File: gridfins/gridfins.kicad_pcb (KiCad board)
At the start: 4 copper layers, 155 parts, among them IC1 2536030320001, J1 RBUS, J2 USB_C_Receptacle_USB2.0, J3 ServoCH0, J4 ServoCH1, J5 ServoCH2, J6 ST1W008S4TR2000, J7 Conn_01x06_Pin, Q1 SSM3K15AMFV,L3F, Q3 DMP3099, Q5 BSZ025N04LS, Q6 BSZ025N04LS, U1 ESP32-S3, U10 LM74810, U2 SN65HVD230, U3 LM66200DRLR, U4 MAX77827AEFD+T, U5 SC4215ASTRT, U6 SiC437AED-T1, U8 MMC5983MA, U9 H3LIS331DLTR, Y1 R940000171

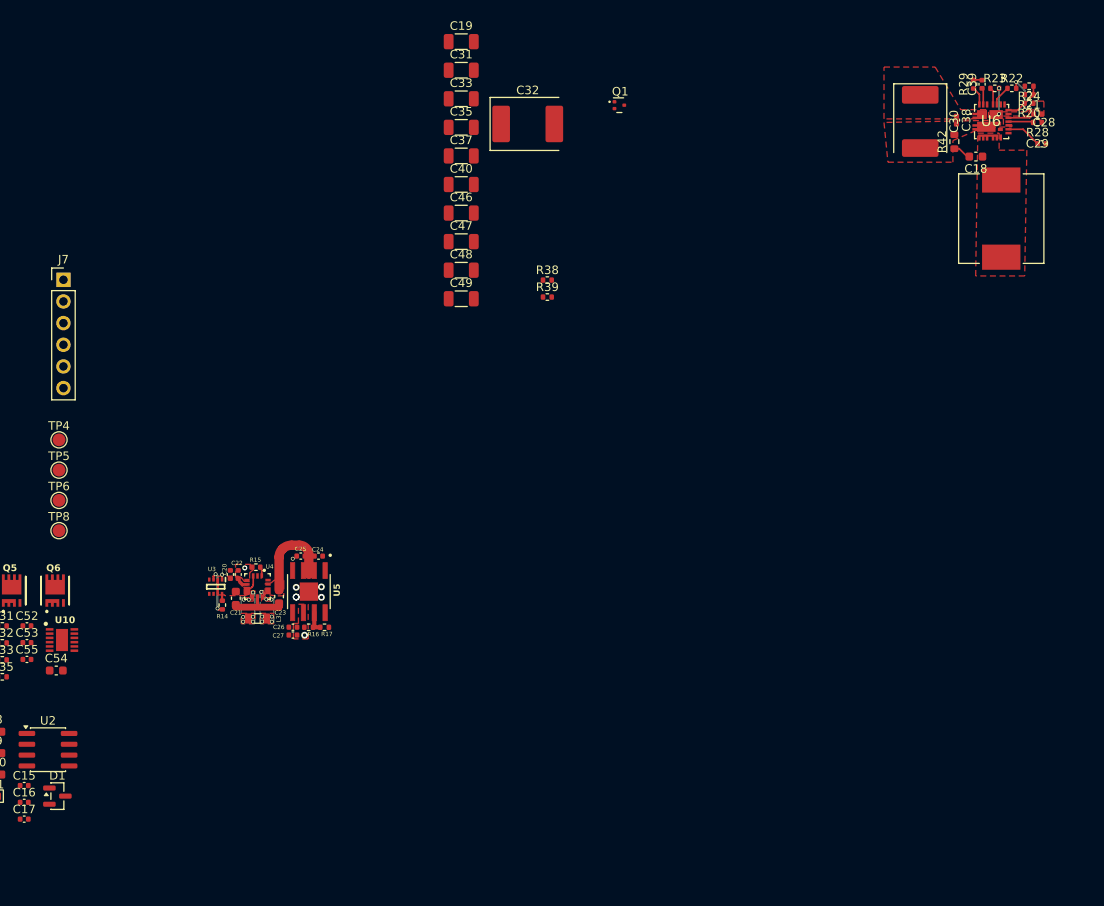
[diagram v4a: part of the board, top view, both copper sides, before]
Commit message: PCB + schematic updates
Solved footprint error which prevented PCB from updating

Deleted old buck converter PCB design (old buck now replaced with 2 for servo and linear acc)

Moved Snubber and crossed out capacitor network to the backside of board

Unsure whether if the +10V routing is valid - currently connected via tracers, not planes (may be a problem for current)

Restructured old pcb which previously had planes associated with no nets (assigned nets to them)

If current design approved, will proceed to carry out the same design for the servo controlling buck converter.
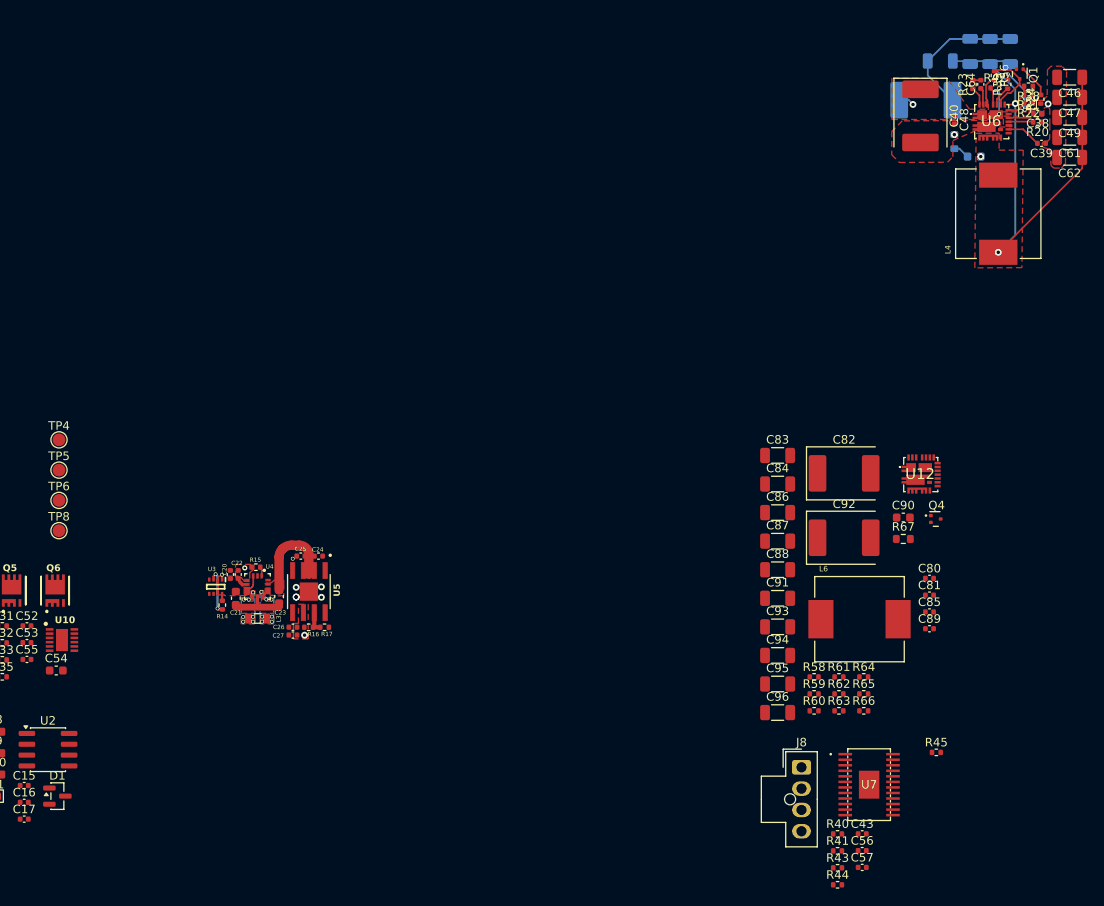
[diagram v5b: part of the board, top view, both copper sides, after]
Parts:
- removed C18: 160pF, Capacitor_SMD:C_0603_1608Metric
- removed C19, C31, C33, C35, C37: 47uF, Capacitor_SMD:C_1206_3216Metric
- removed C28: 1uF, Capacitor_SMD:C_0402_1005Metric
- removed C29: 4.7uF, Capacitor_SMD:C_0402_1005Metric
- removed C30, C32: 100uF, Capacitor_Tantalum_SMD:CP_EIA-7360-38_Kemet-E
- removed J7: Conn_01x06_Pin, Connector_PinHeader_2.54mm:PinHeader_1x06_P2.54mm_Vertical
- removed R28: 10k, Resistor_SMD:R_0402_1005Metric
- removed R29: 2.2, Resistor_SMD:R_0402_1005Metric
- added C43: 10uF, Capacitor_SMD:C_0402_1005Metric, F.Cu at (243.9, 116.0)
- added C56: 0.01uF, Capacitor_SMD:C_0402_1005Metric, F.Cu at (243.9, 118.0)
- added C57: 2.2uF, Capacitor_SMD:C_0402_1005Metric, F.Cu at (243.9, 120.0)
- added C61: 47uF, Capacitor_SMD:C_1206_3216Metric, F.Cu at (268.2, 34.3)
- added C62: 47uF, Capacitor_SMD:C_1206_3216Metric, F.Cu at (268.2, 36.7)
- added C64: 0.1uF, Capacitor_SMD:C_0402_1005Metric, F.Cu at (257.8, 28.1)
- added C65: 160pF, Capacitor_SMD:C_0603_1608Metric, B.Cu at (257.0, 36.6)
- added C75: 100uF, Capacitor_Tantalum_SMD:CP_EIA-7360-38_Kemet-E, B.Cu at (251.3, 30.0)
- added C76: 47uF, Capacitor_SMD:C_1206_3216Metric, B.Cu at (253.0, 25.4)
- added C77: 47uF, Capacitor_SMD:C_1206_3216Metric, B.Cu at (256.5, 24.3)
- added C78: 47uF, Capacitor_SMD:C_1206_3216Metric, B.Cu at (258.9, 24.3)
- added C79: 47uF, Capacitor_SMD:C_1206_3216Metric, B.Cu at (261.2, 24.3)
- added C80: 1uF, Capacitor_SMD:C_0402_1005Metric, F.Cu at (251.8, 86.0)
- added C81: 4.7uF, Capacitor_SMD:C_0402_1005Metric, F.Cu at (251.8, 88.0)
- added C82: 100uF, Capacitor_Tantalum_SMD:CP_EIA-7360-38_Kemet-E, F.Cu at (241.8, 73.7)
- added C83: 47uF, Capacitor_SMD:C_1206_3216Metric, F.Cu at (233.9, 71.6)
- added C84: 47uF, Capacitor_SMD:C_1206_3216Metric, F.Cu at (233.9, 75.0)
- added C85: 100nF, Capacitor_SMD:C_0402_1005Metric, F.Cu at (251.8, 90.0)
- added C86: 47uF, Capacitor_SMD:C_1206_3216Metric, F.Cu at (233.9, 78.3)
- added C87: 47uF, Capacitor_SMD:C_1206_3216Metric, F.Cu at (233.9, 81.7)
- added C88: 47uF, Capacitor_SMD:C_1206_3216Metric, F.Cu at (233.9, 85.0)
- added C89: 0.1uF, Capacitor_SMD:C_0402_1005Metric, F.Cu at (251.8, 92.0)
- added C90: 160pF, Capacitor_SMD:C_0603_1608Metric, F.Cu at (248.7, 78.9)
- added C91: 47uF, Capacitor_SMD:C_1206_3216Metric, F.Cu at (233.9, 88.4)
- added C92: 100uF, Capacitor_Tantalum_SMD:CP_EIA-7360-38_Kemet-E, F.Cu at (241.8, 81.3)
- added C93: 47uF, Capacitor_SMD:C_1206_3216Metric, F.Cu at (233.9, 91.7)
- added C94: 47uF, Capacitor_SMD:C_1206_3216Metric, F.Cu at (233.9, 95.1)
- added C95: 47uF, Capacitor_SMD:C_1206_3216Metric, F.Cu at (233.9, 98.4)
- added C96: 47uF, Capacitor_SMD:C_1206_3216Metric, F.Cu at (233.9, 101.8)
- added J8: 1053131104, Connector_Molex:Molex_Nano-Fit_105309-xx04_1x04_P2.50mm_Vertical, F.Cu at (236.8, 108.2)
- added L6: 3.3uH, iclr:IND_SPM10065VT-3R3M-D, F.Cu at (243.6, 90.8)
- added Q4: SSM3K15AMFV,L3F, iclr:SOT-723, F.Cu at (252.5, 79.1)
- added R40: 51K, Resistor_SMD:R_0402_1005Metric, F.Cu at (241.0, 116.0)
- added R41: 51K, Resistor_SMD:R_0402_1005Metric, F.Cu at (241.0, 118.0)
- added R43: 0.32, Resistor_SMD:R_0402_1005Metric, F.Cu at (241.0, 120.0)
- added R44: 0.32, Resistor_SMD:R_0402_1005Metric, F.Cu at (241.0, 122.0)
- added R45: 18k, Resistor_SMD:R_0402_1005Metric, F.Cu at (252.6, 106.5)
- added R56: 10k, Resistor_SMD:R_0402_1005Metric, F.Cu at (259.4, 27.1)
- added R57: 5.1R, Resistor_SMD:R_0603_1608Metric, B.Cu at (254.7, 34.8)
- added R58: 10k, Resistor_SMD:R_0402_1005Metric, F.Cu at (238.2, 97.6)
- added R59: 113k, Resistor_SMD:R_0402_1005Metric, F.Cu at (238.2, 99.6)
- added R60: 10k, Resistor_SMD:R_0402_1005Metric, F.Cu at (238.2, 101.6)
- added R61: 2.2, Resistor_SMD:R_0402_1005Metric, F.Cu at (241.1, 97.6)
- added R62: 1k, Resistor_SMD:R_0402_1005Metric, F.Cu at (241.1, 99.6)
- added R63: 442k, Resistor_SMD:R_0402_1005Metric, F.Cu at (241.1, 101.6)
- added R64: 200k, Resistor_SMD:R_0402_1005Metric, F.Cu at (244.1, 97.6)
- added R65: 100k, Resistor_SMD:R_0402_1005Metric, F.Cu at (244.1, 99.6)
- added R66: 10k, Resistor_SMD:R_0402_1005Metric, F.Cu at (244.1, 101.6)
- added R67: 5.1R, Resistor_SMD:R_0603_1608Metric, F.Cu at (248.7, 81.4)
- added U12: SiC437AED-T1, iclr:SiC437BEDT1GE3, F.Cu at (250.7, 73.9)
- added U7: DRV8834PWP, iclr:PWP_24, F.Cu at (244.7, 110.2)
- C38: value 100nF -> 1uF
- C39: value 0.1uF -> 4.7uF
- C40: value 47uF -> 100uF; footprint Capacitor_SMD:C_1206_3216Metric -> Capacitor_Tantalum_SMD:CP_EIA-7360-38_Kemet-E
- C48: value 47uF -> 100nF; footprint Capacitor_SMD:C_1206_3216Metric -> Capacitor_SMD:C_0402_1005Metric
- R21: value 113k -> 157k
- R22: value 200k -> 10k
- R23: value 100k -> 2.2
- R24: value 442k -> 1k
- R38: value 10k -> 442k
- R39: value 1k -> 200k
- R42: value 5.1R -> 100k; footprint Resistor_SMD:R_0603_1608Metric -> Resistor_SMD:R_0402_1005Metric
- moved C49 74.5 mm to (268.2, 32.0), turned to 180 degrees
- moved C47 73.3 mm to (268.2, 29.6), turned to 180 degrees
- moved C46 73.1 mm to (268.2, 27.3), turned to 180 degrees
- moved R38 60.8 mm to (263.4, 28.3), turned to 180 degrees
- moved C48 60.5 mm to (254.7, 32.3), turned to -90 degrees
- moved R39 59.5 mm to (260.9, 28.1), turned to 90 degrees
- moved C40 54.5 mm to (250.7, 31.8), turned to -90 degrees
- moved Q1 47.1 mm to (262.4, 26.9), turned to -90 degrees
- moved C39 9.83 mm to (264.9, 35.0), turned to 180 degrees
- moved C38 9.55 mm to (264.4, 31.5), turned to 180 degrees
- moved R42 7.89 mm to (259.4, 28.5), turned to 0 degrees
- moved R22 2.62 mm to (263.4, 30.3), turned to 180 degrees
- moved R23 2.60 mm to (256.9, 28.1), turned to 90 degrees
- moved R20 2.42 mm to (264.4, 32.5)
- moved R24 2.04 mm to (264.8, 29.9), turned to 90 degrees
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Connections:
- net /Buck/SW renamed /Buck_H_bridge/SW
- C38 pad 1: /VOUTSwitch -> GND
- C38 pad 2: GND -> /Buck_H_bridge/VDD
- C39 pad 1: /Buck/BOOT -> GND
- C39 pad 2: Net-(C39-Pad2) -> Net-(U6-V_DRV)
- C40 pad 1: +7.4V -> +16.8V
- C46 pad 1: +7.4V -> +10V
- C47 pad 1: +7.4V -> +10V
- C48 pad 1: +7.4V -> +16.8V
- C49 pad 1: +7.4V -> +10V
- C52 pad 1: +16.8V -> +10V
- L4 pad 1: +7.4V -> +10V
- Q1 pad 3: /Buck/EN -> /Buck_H_bridge/EN
- Q5 pad 1: +16.8V -> +10V
- Q5 pad 2: +16.8V -> +10V
- Q5 pad 3: +16.8V -> +10V
- Q5 pad A1: +16.8V -> +10V
- R20 pad 1: GND -> /Buck_H_bridge/VDD
- R20 pad 2: /Buck/FB -> /BuckPGOOD
- R21 pad 1: /Buck/FB -> /Buck_H_bridge/FB
- R21 pad 2: +7.4V -> +10V
- R22 pad 1: Net-(U6-MODE_2) -> GND
- R22 pad 2: /Buck/VDD -> /Buck_H_bridge/FB
- R23 pad 1: Net-(U6-_MODE_1) -> /Buck_H_bridge/PHASE
- R23 pad 2: GND -> Net-(C64-Pad2)
- R24 pad 1: /Buck/FB -> GND
- R24 pad 2: +7.4V -> /BUCK_EN
- R38 pad 1: /Buck/EN -> /Buck_H_bridge/FB
- R38 pad 2: /VOUTSwitch -> +10V
- R39 pad 1: GND -> Net-(U6-MODE_2)
- R39 pad 2: /BUCK_EN -> /Buck_H_bridge/VDD
- R42 pad 1: Net-(C18-Pad2) -> Net-(U6-_MODE_1)
- U1 pad 21: unconnected-(U1-GPIO15/ADC2_CH4/XTAL_32K_P-Pad21) -> /STEP/BENBL
- U1 pad 22: unconnected-(U1-GPIO16/ADC2_CH5/XTAL_32K_N-Pad22) -> /NSLEEP
- U1 pad 23: unconnected-(U1-GPIO17/ADC2_CH6/DAC_2-Pad23) -> /M0/APHASE
- U1 pad 24: unconnected-(U1-GPIO18/ADC2_CH7/DAC_1-Pad24) -> /DIR/BPHASE
- U1 pad 27: unconnected-(U1-GPIO21-Pad27) -> /NENBL/AENBL
- U10 pad 2: +16.8V -> +10V
- U10 pad 3: +16.8V -> +10V
- U6 pad 1: /VOUTSwitch -> +16.8V
- U6 pad 15: /Buck/VDD -> /Buck_H_bridge/VDD
- U6 pad 17: /Buck/FB -> /Buck_H_bridge/FB
- U6 pad 18: +7.4V -> +10V
- U6 pad 19: /Buck/EN -> /Buck_H_bridge/EN
- U6 pad 2: /VOUTSwitch -> +16.8V
- U6 pad 22: /VOUTSwitch -> +16.8V
- U6 pad 23: /Buck/BOOT -> /Buck_H_bridge/BOOT
- U6 pad 24: /Buck/PHASE -> /Buck_H_bridge/PHASE
- U6 pad 26: /VOUTSwitch -> +16.8V
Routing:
- net +10V: track 0.00 -> 59.4 mm, vias 0 -> 2
- net GND: track 10.3 -> 27.2 mm, vias 10 -> 12
- net /Buck_H_bridge/VDD: track 0.00 -> 11.5 mm, vias 0 -> 2
- net /Buck/VDD: track 10.2 -> 0.00 mm, vias 2 -> 0
- net /Buck_H_bridge/EN: track 0.00 -> 7.61 mm
- net +16.8V: track 0.00 -> 5.42 mm, vias 0 -> 1
- net /Buck_H_bridge/FB: track 0.00 -> 4.68 mm
- net /Buck/FB: track 4.68 -> 0.00 mm
- net /BUCK_EN: track 0.00 -> 3.86 mm
- net Net-(C65-Pad2): track 0.00 -> 2.23 mm
- net /Buck_H_bridge/PHASE: track 0.00 -> 2.16 mm
- net /Buck/PHASE: track 2.15 -> 0.00 mm
- net Net-(C18-Pad2): track 2.13 -> 0.00 mm
- net /Buck_H_bridge/BOOT: track 0.00 -> 2.02 mm
- net /Buck/BOOT: track 1.95 -> 0.00 mm
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- added copper zone on F.Cu, net +16.8V
- removed copper zone on F.Cu, net /VOUTSwitch

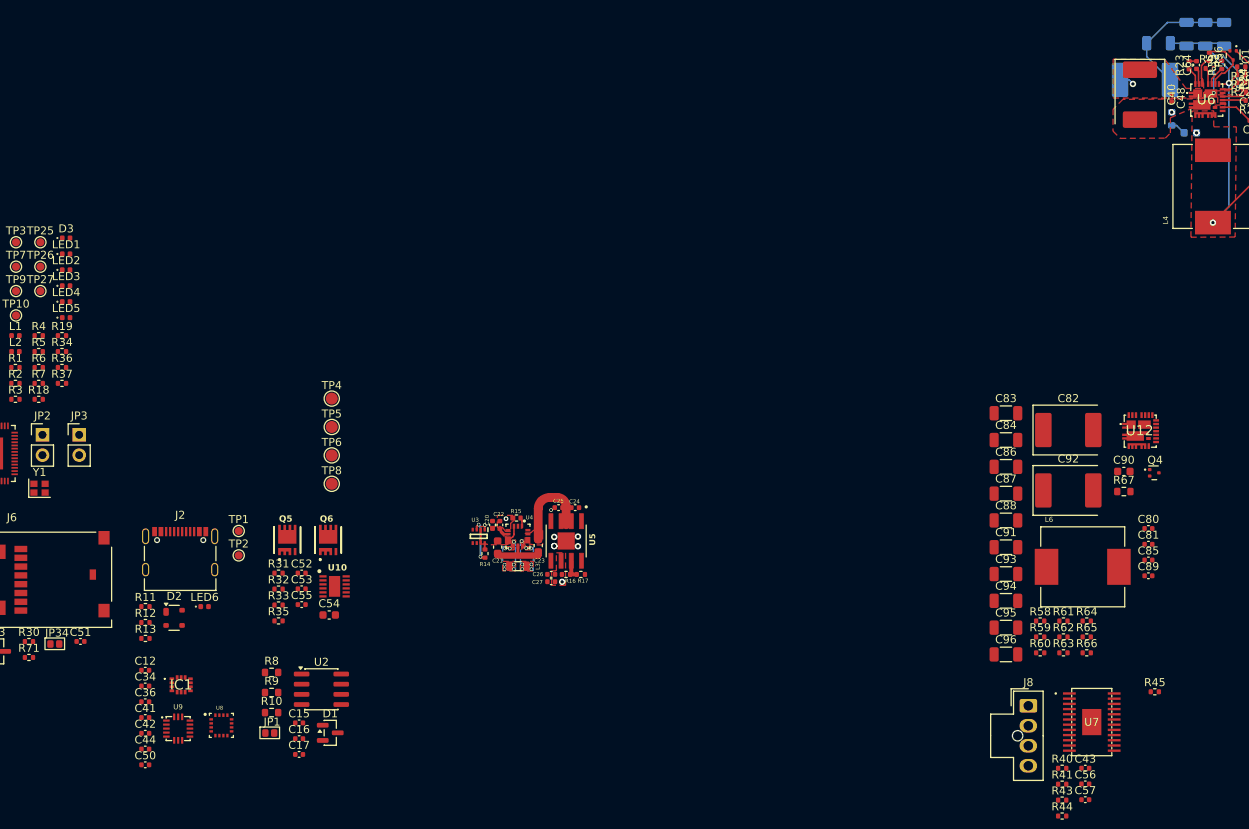
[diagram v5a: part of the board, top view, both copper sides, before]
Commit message: Handoff
implemented changes advised by Will. Still a bit unsure about how the EPAD should be connected to ground. The PCB design of both buck converters for servo and Hbridge(linear accuator) was completed - but still needs to be reviewed
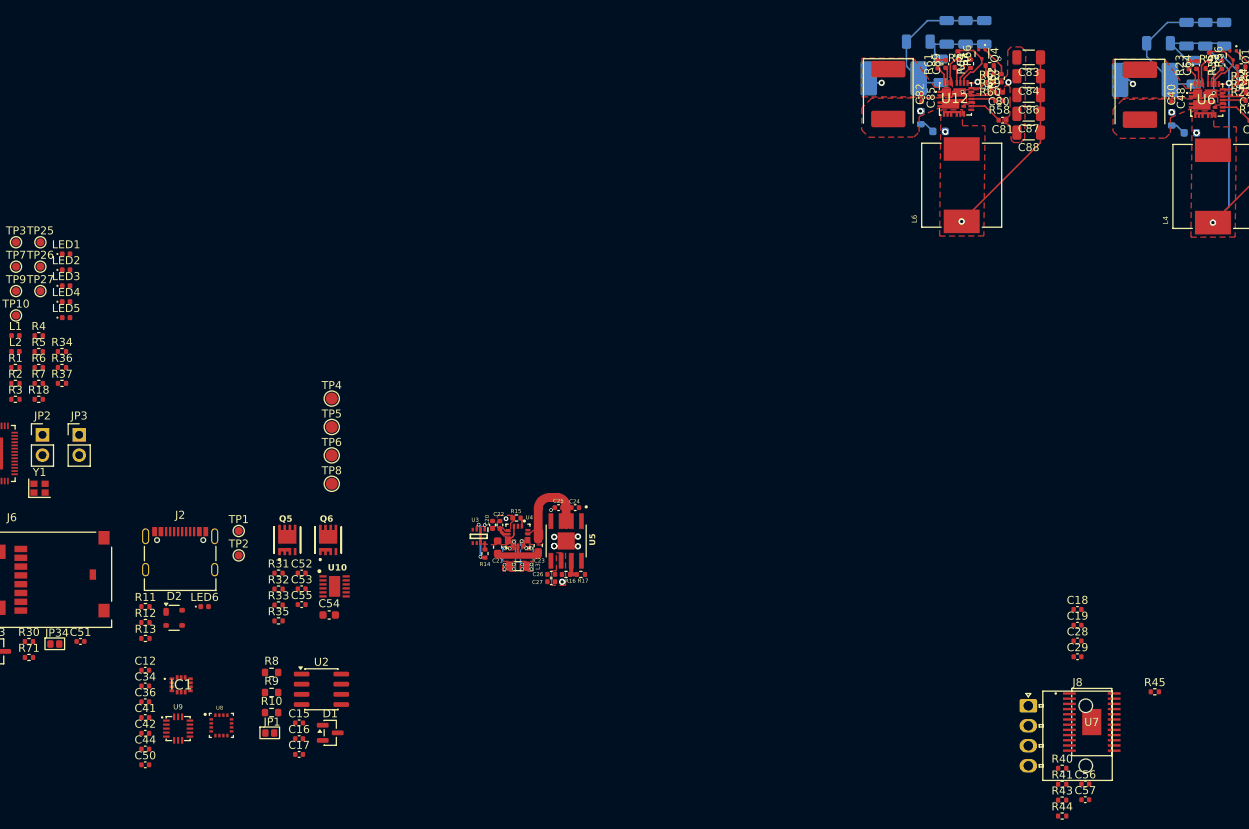
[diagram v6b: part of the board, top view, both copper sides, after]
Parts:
- removed C43: 10uF, Capacitor_SMD:C_0402_1005Metric
- removed D3: LED, LED_SMD:LED_0402_1005Metric
- removed R19: R, Resistor_SMD:R_0402_1005Metric
- added C18: 10uF, Capacitor_SMD:C_0402_1005Metric, F.Cu at (242.9, 96.2)
- added C19: 0.01uF, Capacitor_SMD:C_0402_1005Metric, F.Cu at (242.9, 98.1)
- added C28: 0.1uF, Capacitor_SMD:C_0402_1005Metric, F.Cu at (242.9, 100.1)
- added C29: 1uF, Capacitor_SMD:C_0402_1005Metric, F.Cu at (242.9, 102.1)
- added C66: 47uF, Capacitor_SMD:C_1206_3216Metric, B.Cu at (257.4, 29.0)
- C90, C91, C92, C93, C94, C95, C96, R67: moved to B.Cu
- J8: footprint Connector_Molex:Molex_Nano-Fit_105309-xx04_1x04_P2.50mm_Vertical -> Connector_Molex:Molex_Nano-Fit_105313-xx04_1x04_P2.50mm_Horizontal
- R38: value 442k -> 0
- moved C96 78.1 mm to (226.5, 24.0), turned to 90 degrees
- moved R66 76.4 mm to (227.9, 26.9), turned to -90 degrees
- moved C95 74.6 mm to (228.9, 24.0), turned to 90 degrees
- moved R63 74.0 mm to (231.9, 28.2), turned to 180 degrees
- moved R65 73.0 mm to (228.0, 28.4)
- moved R60 71.6 mm to (231.9, 30.3), turned to 180 degrees
- moved R61 71.3 mm to (225.4, 28.0), turned to 90 degrees
- moved R64 71.1 mm to (229.5, 28.0), turned to 90 degrees
- moved C94 71.1 mm to (231.2, 24.0), turned to 90 degrees
- moved R59 70.7 mm to (231.9, 29.2), turned to 180 degrees
- moved R62 70.3 mm to (233.4, 29.8), turned to 90 degrees
- moved C89 68.8 mm to (226.4, 28.0), turned to 90 degrees
- moved C93 67.4 mm to (223.0, 25.2), turned to 180 degrees
- moved R58 65.2 mm to (233.1, 32.6), turned to 180 degrees
- moved C85 64.4 mm to (223.4, 32.2), turned to -90 degrees
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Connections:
- net Net-(U7-AVREF) renamed /Linear Actuator/VREFO
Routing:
- net +7.4V: track 0.00 -> 37.4 mm, vias 0 -> 2
- net GND: track 27.2 -> 49.4 mm, vias 12 -> 16
- net /Buck_SERVO/EN: track 0.00 -> 7.61 mm
- net /Buck_SERVO/VDD: track 0.00 -> 6.45 mm, vias 0 -> 2
- net +16.8V: track 5.42 -> 10.8 mm, vias 1 -> 2
- net /Buck_SERVO/FB: track 0.00 -> 4.68 mm
- net Net-(U12-V_DRV): track 0.00 -> 4.12 mm
- net /BUCK_EN: track 3.86 -> 7.73 mm
- net +10V: track 59.4 -> 63.2 mm
- net /BuckPGOOD: track 2.93 -> 5.86 mm
- net Net-(U12-MODE_2): track 0.00 -> 2.40 mm
- net /Buck_SERVO/PHASE: track 0.00 -> 2.16 mm
- net /Buck_SERVO/BOOT: track 0.00 -> 2.02 mm
- net Net-(U12-_MODE_1): track 0.00 -> 2.02 mm
- net Net-(C90-Pad2): track 0.00 -> 1.87 mm
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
